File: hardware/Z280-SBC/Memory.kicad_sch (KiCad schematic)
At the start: 9 parts, among them U1 74HC14, U5 74HC138, U6 74HC08, U7 M29F800, U8 AS6C8016

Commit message: Mostly done Rev1
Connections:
- net 0SEL is gone; now on net ~{0SEL}: JP5.1 (A)
- net 2SEL is gone; now on net ~{2SEL}: JP5.3 (B)
- net ROMSEL is gone; now on net ~{ROMSEL}: JP5.2 (C)
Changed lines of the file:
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@@
     )
   )
-  (global_label "0SEL" (shape input) (at 107.95 52.07 180) (fields_autoplaced)
+  (global_label "~{0SEL}" (shape input) (at 107.95 52.07 180) (fields_autoplaced)
     (effects (font (size 1.27 1.27)) (justify right))
-    (property "Intersheet References" "${INTERSHEET_REFS}" (id 0) (at 184.15 -29.21 0)
-      (effects (font (size 1.27 1.27)) (justify left) hide)
+    (property "Intersheet References" "${INTERSHEET_REFS}" (id 0) (at 100.9407 51.9906 0)
+      (effects (font (size 1.27 1.27)) (justify right) hide)
     )
   )
@@
     )
   )
-  (global_label "ROMSEL" (shape output) (at 120.65 58.42 0) (fields_autoplaced)
+  (global_label "~{ROMSEL}" (shape output) (at 120.65 58.42 0) (fields_autoplaced)
     (effects (font (size 1.27 1.27)) (justify left))
-    (property "Intersheet References" "${INTERSHEET_REFS}" (id 0) (at 184.15 -29.21 0)
+    (property "Intersheet References" "${INTERSHEET_REFS}" (id 0) (at 130.5017 58.3406 0)
       (effects (font (size 1.27 1.27)) (justify left) hide)
     )
   )
-  (global_label "2SEL" (shape input) (at 107.95 64.77 180) (fields_autoplaced)
+  (global_label "~{2SEL}" (shape input) (at 107.95 64.77 180) (fields_autoplaced)
     (effects (font (size 1.27 1.27)) (justify right))
-    (property "Intersheet References" "${INTERSHEET_REFS}" (id 0) (at 184.15 -29.21 0)
-      (effects (font (size 1.27 1.27)) (justify left) hide)
+    (property "Intersheet References" "${INTERSHEET_REFS}" (id 0) (at 100.9407 64.6906 0)
+      (effects (font (size 1.27 1.27)) (justify right) hide)
     )
   )

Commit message: Rev1 - All connections completed
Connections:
- net +5V: now also U7.12 (~{RST})
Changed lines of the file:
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@@
   (junction (at 49.53 21.59) (diameter 0) (color 0 0 0 0)
   )
+  (junction (at 198.12 105.41) (diameter 0) (color 0 0 0 0)
+  )
   (junction (at 209.55 17.78) (diameter 0) (color 0 0 0 0)
   )
@@
     (stroke (width 0) (type default) (color 0 0 0 0))
   )
+  (wire (pts (xy 195.58 102.87) (xy 198.12 102.87))
+    (stroke (width 0) (type default) (color 0 0 0 0))
+  )
   (bus (pts (xy 266.7 74.93) (xy 266.7 77.47))
     (stroke (width 0) (type default) (color 0 0 0 0))
@@
     (stroke (width 0) (type default) (color 0 0 0 0))
   )
-  (wire (pts (xy 195.58 105.41) (xy 209.55 105.41))
+  (wire (pts (xy 195.58 105.41) (xy 198.12 105.41))
+    (stroke (width 0) (type default) (color 0 0 0 0))
+  )
+  (wire (pts (xy 198.12 102.87) (xy 198.12 105.41))
     (stroke (width 0) (type default) (color 0 0 0 0))
   )
@@
     (stroke (width 0) (type default) (color 0 0 0 0))
   )
+  (wire (pts (xy 198.12 105.41) (xy 209.55 105.41))
+    (stroke (width 0) (type default) (color 0 0 0 0))
+  )

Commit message: Z280-SBC Revision 1 is complete
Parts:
- U7: value M29F800 -> M29F160
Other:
- title: (none) -> Z280-SBC
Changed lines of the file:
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@@
 (kicad_sch (version 20211123) (generator eeschema)
   (paper "A4")
+  (title_block
+    (title "Z280-SBC")
+    (rev "1")
+  )
   (junction (at 240.03 46.99) (diameter 0) (color 0 0 0 0)
   )
@@
       (effects (font (size 1.27 1.27)) (justify left))
     )
-    (property "Value" "M29F800" (id 1) (at 184.8994 46.99 0)
+    (property "Value" "M29F160" (id 1) (at 184.8994 46.99 0)
       (effects (font (size 1.27 1.27)) (justify left))
     )

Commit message: Fixed most of the issues with Rev.1
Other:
- note added: "ADDRESS DECODE"
- note added: "UPPER/LOWER BYTE SELECT"
- moved on the sheet: JP2, JP3, JP4, JP5, U1D, U5, U6A, U6B, U6C, U6D

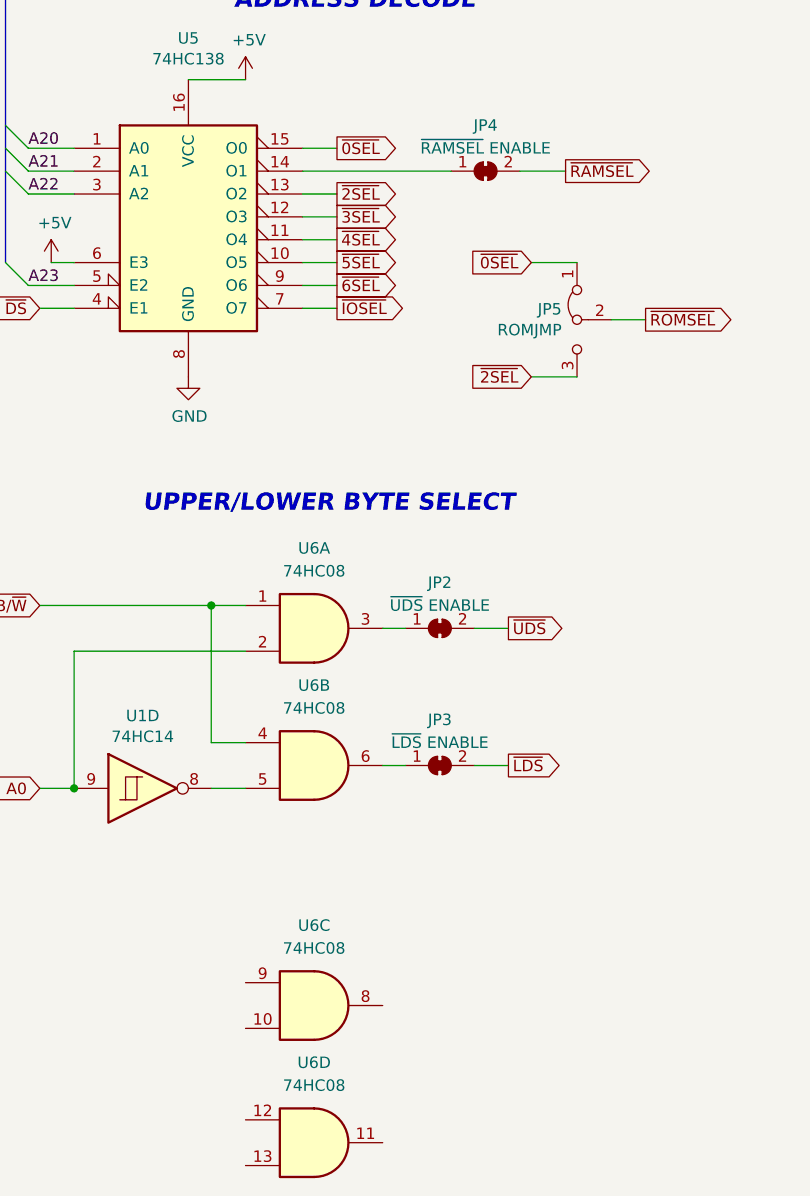
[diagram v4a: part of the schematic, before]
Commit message: Added computie-kicad-library and fixed references to point to it
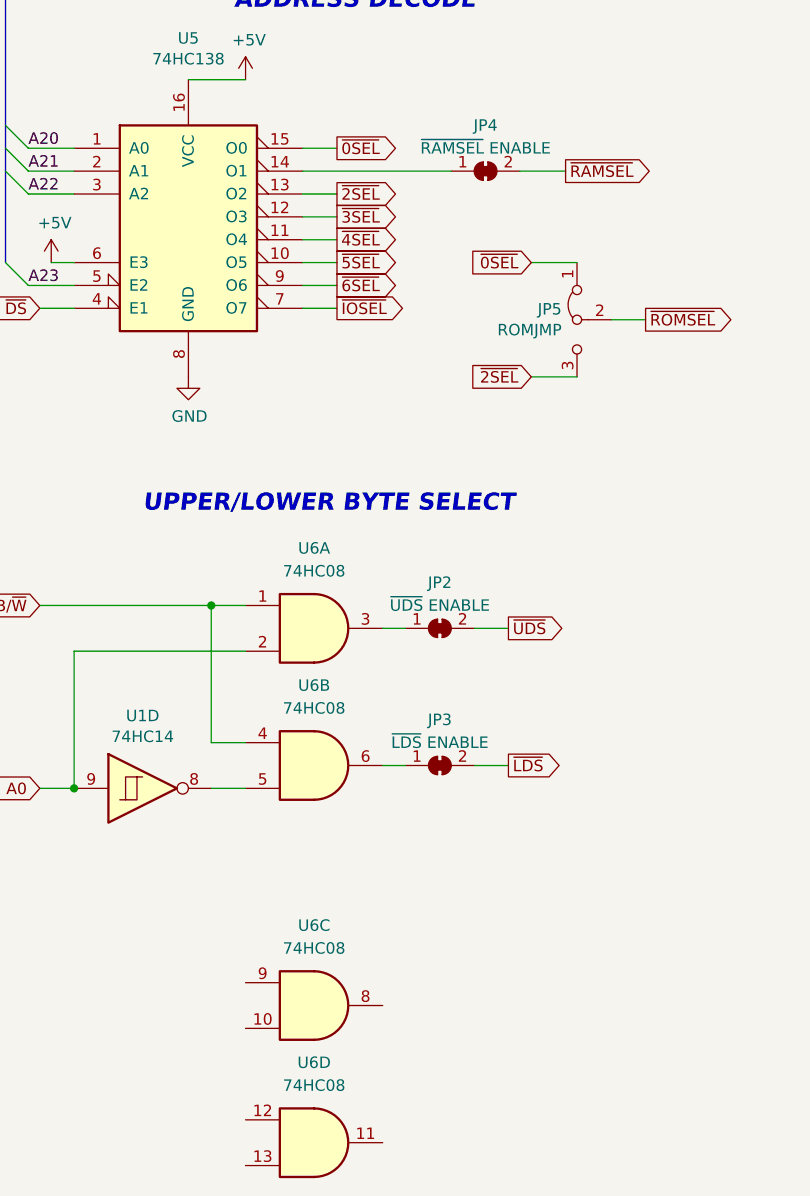
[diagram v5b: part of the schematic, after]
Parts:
- U7: symbol Z280:M29F160 -> Computie_Memory:M29F160-N
- U8: symbol Z280:AS6C8016 -> Computie_Memory:AS6C8016-55ZIN
